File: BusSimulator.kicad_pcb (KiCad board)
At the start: 2 copper layers, 15 parts, among them U1 MPM3620, U2 MPM3620

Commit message: Finished 3v3 and 5V
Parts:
- moved R6 101.2 mm to (114.3, 123.9), turned to 270 degrees
- moved R5 97.3 mm to (114.3, 120.7), turned to 270 degrees
- moved R7 86.7 mm to (117.6, 116.1), turned to 270 degrees
- moved R8 79.0 mm to (114.8, 116.7), turned to 180 degrees
- moved C4 58.7 mm to (126.2, 120.9), turned to 270 degrees
- moved C3 54.3 mm to (122.3, 115.2), turned to 180 degrees
- moved U2 53.3 mm to (118.2, 121.8), turned to 0 degrees
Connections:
- C3 pad 1: Earth -> GNDREF
- C4 pad 1: Earth -> GNDREF
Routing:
- net (no net): track 9.47 -> 37.8 mm, vias 6 -> 2
- net GNDREF: track 13.5 -> 39.7 mm
- net Net-(C1-Pad2): track 8.35 -> 30.4 mm
- net GNDA: track 13.9 -> 29.0 mm
- net +3V3: track 0.00 -> 10.7 mm, vias 0 -> 4
- net Net-(C3-Pad2): track 0.00 -> 8.35 mm
- net Net-(R5-Pad2): track 0.00 -> 4.66 mm
- net Net-(R8-Pad1): track 0.00 -> 3.17 mm
- net Net-(R7-Pad2): track 0.00 -> 2.36 mm
- net +5V: track 25.3 -> 26.9 mm, vias 3 -> 4
- added copper zone on B.Cu, net +3V3
- added copper zone on F.Cu, net +3V3
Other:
- board text added: "Vin"

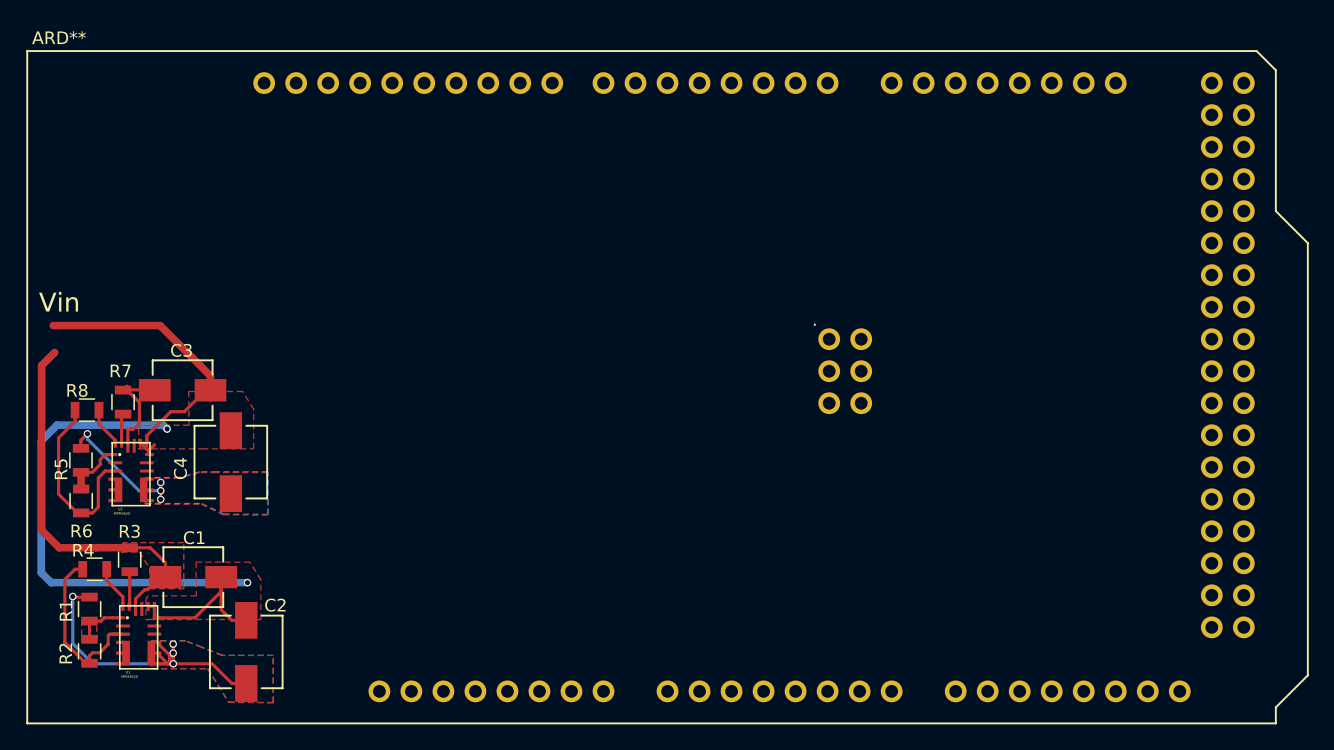
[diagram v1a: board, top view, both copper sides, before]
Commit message: added dc connector and outline pcb
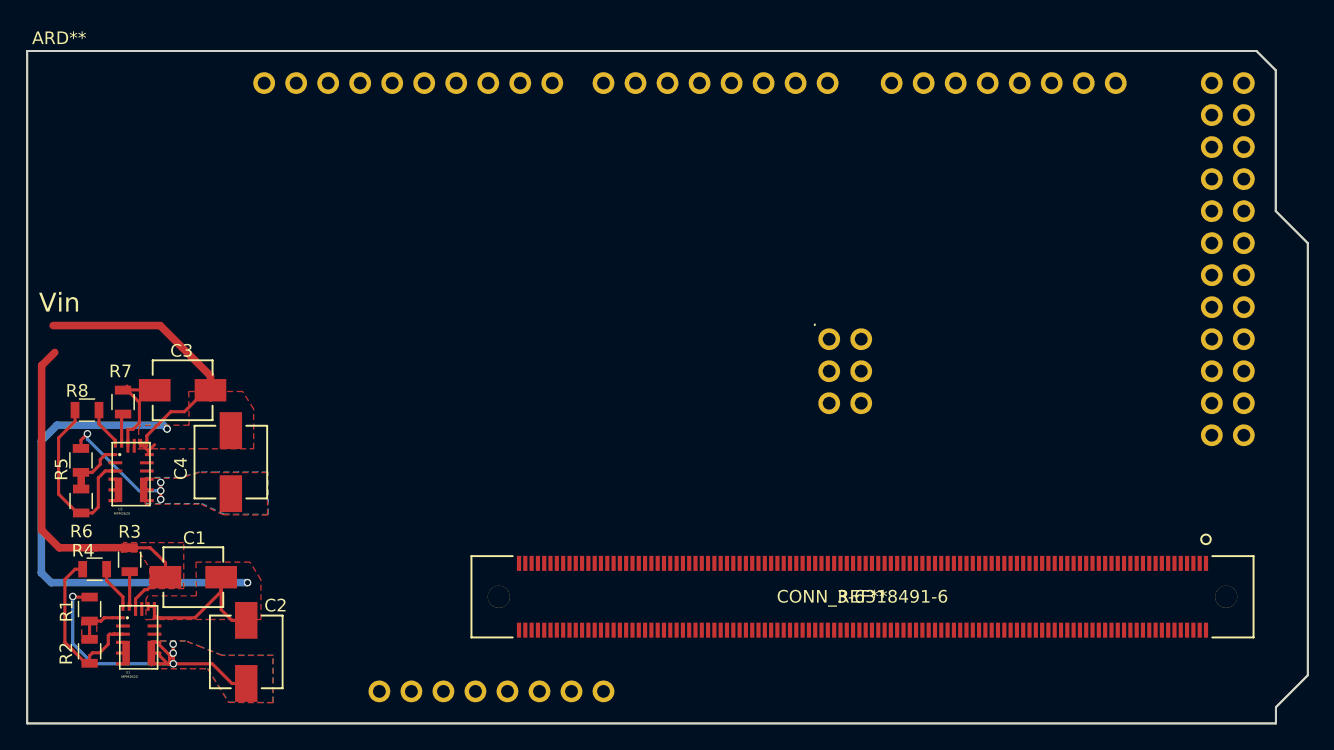
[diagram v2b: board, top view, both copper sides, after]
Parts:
- added REF**: CONN_3-6318491-6, BusSimulator:ComExpressMini10, F.Cu at (211.0, 134.2)
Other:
- board outline added: 101.6 x 53.3 mm

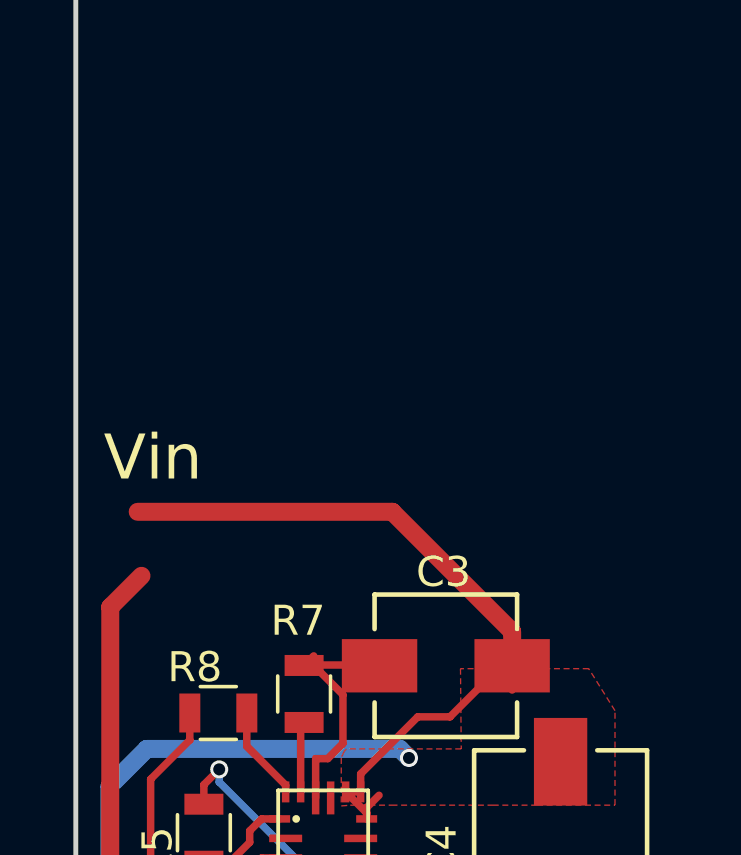
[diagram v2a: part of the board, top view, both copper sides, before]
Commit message: dc jack
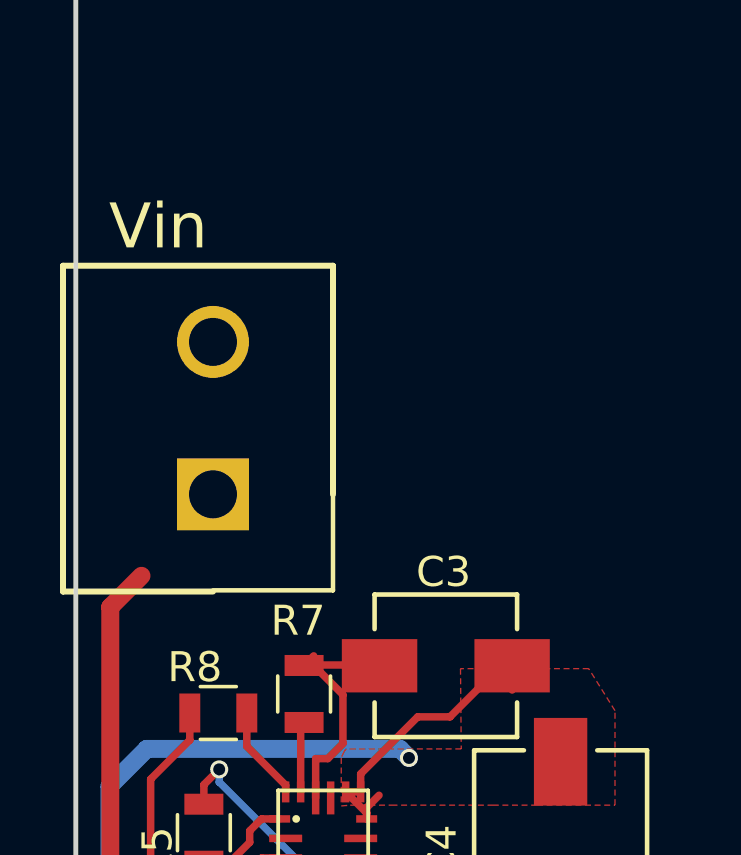
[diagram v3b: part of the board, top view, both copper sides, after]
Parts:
- added J1: , BusSimulator:OSTTA024163, F.Cu at (114.6, 109.5)
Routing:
- net GNDREF: track 39.7 -> 24.4 mm
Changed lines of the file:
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@@
     (thickness 1.6)
     (drawings 10)
-    (tracks 144)
+    (tracks 141)
     (zones 0)
-    (modules 16)
+    (modules 17)
     (nets 23)
   )
@@
     (mod_text_size 1 1)
     (mod_text_width 0.15)
-    (pad_size 1.524 1.524)
-    (pad_drill 0.762)
+    (pad_size 2.4 2.4)
+    (pad_drill 1.6)
     (pad_to_mask_clearance 0.2)
     (aux_axis_origin 0 0)
@@
     (pad 222 thru_hole circle (at 5.871598 2.65 180) (size 1.7526 1.7526) (drill 1.7526) (layers *.Cu F.SilkS))
   )
+  (module BusSimulator:OSTTA024163 (layer F.Cu)
+    (at 114.575 109.45 90)
+    (descr OSTTA024163)
+    (tags Connector)
+    (fp_text reference J1 (at 2.55 -0.15 360) (layer F.SilkS) hide
+      (effects (font (size 1.27 1.27) (thickness 0.254)))
+    )
+    (fp_text value "" (at 0 0 90) (layer F.SilkS) hide
+      (effects (font (size 1.27 1.27) (thickness 0.254)))
+    )
+    (fp_line (start -3.2 0) (end -3.2 4) (layer F.SilkS) (width 0.15))
+    (fp_line (start -3.2 4) (end 1 4) (layer F.SilkS) (width 0.15))
+    (fp_line (start -3.49 4.25) (end -3.49 -5.25) (layer Dwgs.User) (width 0.05))
+    (fp_line (start -3.49 -5.25) (end 7.87 -5.25) (layer Dwgs.User) (width 0.05))
+    (fp_line (start 7.87 -5.25) (end 7.87 4.25) (layer Dwgs.User) (width 0.05))
+    (fp_line (start 7.87 4.25) (end -3.49 4.25) (layer Dwgs.User) (width 0.05))
+    (fp_line (start -3.24 4) (end -3.24 -5) (layer Dwgs.User) (width 0.1))
+    (fp_line (start -3.24 -5) (end 7.62 -5) (layer Dwgs.User) (width 0.1))
+    (fp_line (start 7.62 -5) (end 7.62 4) (layer Dwgs.User) (width 0.1))
+    (fp_line (start 7.62 4) (end -3.24 4) (layer Dwgs.User) (width 0.1))
+    (fp_line (start 0 4) (end 7.62 4) (layer F.SilkS) (width 0.2))
+    (fp_line (start 7.62 4) (end 7.62 -5) (layer F.SilkS) (width 0.2))
+    (fp_line (start 7.62 -5) (end -3.24 -5) (layer F.SilkS) (width 0.2))
+    (fp_line (start -3.24 -5) (end -3.24 0) (layer F.SilkS) (width 0.2))
+    (pad 1 thru_hole rect (at 0 0 180) (size 2.4 2.4) (drill 1.6) (layers *.Cu *.Mask F.SilkS))
+    (pad 2 thru_hole circle (at 5.08 0 180) (size 2.4 2.4) (drill 1.6) (layers *.Cu *.Mask F.SilkS))
+  )
   (gr_line (start 110 141.6) (end 110 88.25) (layer Edge.Cuts) (width 0.15))
   (gr_line (start 209.075 141.6) (end 110 141.6) (layer Edge.Cuts) (width 0.15))
@@
   (gr_line (start 207.525 88.25) (end 209.05 89.775) (layer Edge.Cuts) (width 0.15))
   (gr_line (start 110 88.25) (end 207.525 88.25) (layer Edge.Cuts) (width 0.15))
-  (gr_text "Vin \n" (at 112.5728 108.2294) (layer F.SilkS)
+  (gr_text "Vin \n" (at 112.75 100.525 360) (layer F.SilkS)
     (effects (font (size 1.5 1.5) (thickness 0.3)))
   )
@@
   (segment (start 116.996948 119.144698) (end 115.701948 117.849698) (width 0.25) (layer F.Cu) (net 11))
   (segment (start 115.701948 117.849698) (end 115.701948 116.739698) (width 0.25) (layer F.Cu) (net 11))
-  (segment (start 120.55305 110.0328) (end 112.0648 110.0328) (width 0.6) (layer F.Cu) (net 17))
-  (segment (start 124.546148 115.164898) (end 124.546148 114.025898) (width 0.6) (layer F.Cu) (net 17))
-  (segment (start 124.546148 114.025898) (end 120.55305 110.0328) (width 0.6) (layer F.Cu) (net 17))
   (segment (start 119.696948 119.894698) (end 119.696948 120.269698) (width 0.25) (layer F.Cu) (net 17))
   (segment (start 119.696948 119.894698) (end 120.110046 119.4816) (width 0.25) (layer F.Cu) (net 17))

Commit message: POWER SUPPLY STUFF
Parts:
- J1: value (none) -> CONN_3-6318491-6
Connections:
- C1 pad 2: Net-(C1-Pad2) -> +12V
- C3 pad 2: Net-(C3-Pad2) -> +12V
- J1 pad 1: (no net) -> +12V
- J1 pad 2: (no net) -> GNDREF
- R3 pad 1: Net-(C1-Pad2) -> +12V
- R7 pad 1: Net-(C3-Pad2) -> +12V
- U1 pad 16: Net-(C1-Pad2) -> +12V
- U2 pad 16: Net-(C3-Pad2) -> +12V
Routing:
- net +12V: track 0.00 -> 52.2 mm
- net GNDREF: track 24.4 -> 58.9 mm
- net Net-(C1-Pad2): track 30.4 -> 0.00 mm
- net (no net): track 37.8 -> 53.7 mm, vias 2 -> 4
- net Net-(C3-Pad2): track 8.35 -> 0.00 mm
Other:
- net class Default: trace_width 0.25 -> 0.6

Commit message: CONNECTOR MAPPED
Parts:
- renumbered REF** to J1, J1 to J2
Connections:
- J1 pad 1: (no net) -> GND
- J1 pad 10: (no net) -> GBE0_MDI1+
- J1 pad 100: (no net) -> GND
- J1 pad 101: (no net) -> Net-(J1-Pad101)
- J1 pad 102: (no net) -> Net-(J1-Pad102)
- J1 pad 103: (no net) -> LIDn
- J1 pad 104: (no net) -> VCC_12V
- J1 pad 105: (no net) -> VCC_12V
- J1 pad 106: (no net) -> VCC_12V
- J1 pad 107: (no net) -> VCC_12V
- J1 pad 108: (no net) -> VCC_12V
- J1 pad 109: (no net) -> VCC_12V
- J1 pad 11: (no net) -> GND
- J1 pad 110: (no net) -> GND
- J1 pad 111: (no net) -> GND
- J1 pad 112: (no net) -> GBE0_ACTn
- J1 pad 113: (no net) -> Net-(J1-Pad113)
- J1 pad 114: (no net) -> Net-(J1-Pad114)
- J1 pad 115: (no net) -> Net-(J1-Pad115)
- J1 pad 116: (no net) -> Net-(J1-Pad116)
- J1 pad 117: (no net) -> Net-(J1-Pad117)
- J1 pad 118: (no net) -> Net-(J1-Pad118)
- J1 pad 119: (no net) -> Net-(J1-Pad119)
- J1 pad 12: (no net) -> GBE0_MDI0-
- J1 pad 120: (no net) -> Net-(J1-Pad120)
- J1 pad 121: (no net) -> GND
- J1 pad 122: (no net) -> PWRBTNn
- J1 pad 123: (no net) -> Net-(J1-Pad123)
- J1 pad 124: (no net) -> Net-(J1-Pad124)
- J1 pad 125: (no net) -> Net-(J1-Pad125)
- J1 pad 126: (no net) -> Net-(J1-Pad126)
- J1 pad 127: (no net) -> Net-(J1-Pad127)
- J1 pad 128: (no net) -> Net-(J1-Pad128)
- J1 pad 129: (no net) -> Net-(J1-Pad129)
- J1 pad 13: (no net) -> GBE0_MDI0+
- J1 pad 130: (no net) -> Net-(J1-Pad130)
- J1 pad 131: (no net) -> GND
- J1 pad 132: (no net) -> USB_SSTX0-
- J1 pad 133: (no net) -> USB_SSTX0+
- J1 pad 134: (no net) -> PWR_OK
- J1 pad 135: (no net) -> Net-(J1-Pad135)
- J1 pad 136: (no net) -> Net-(J1-Pad136)
- J1 pad 137: (no net) -> Net-(J1-Pad137)
- J1 pad 138: (no net) -> Net-(J1-Pad138)
- J1 pad 139: (no net) -> Net-(J1-Pad139)
- J1 pad 14: (no net) -> GBE0_CTREF(GND)
- J1 pad 140: (no net) -> AC/HDA_SDIN0
- J1 pad 141: (no net) -> GND
- J1 pad 142: (no net) -> Net-(J1-Pad142)
- J1 pad 143: (no net) -> I2C_CK
- J1 pad 144: (no net) -> I2C_DAT
- J1 pad 145: (no net) -> THRMn
- J1 pad 146: (no net) -> Net-(J1-Pad146)
- J1 pad 147: (no net) -> Net-(J1-Pad147)
- J1 pad 148: (no net) -> USB_4_5_OCn
- J1 pad 149: (no net) -> USB5-
- J1 pad 15: (no net) -> Net-(J1-Pad15)
- J1 pad 150: (no net) -> USB5+
- J1 pad 151: (no net) -> GND
- J1 pad 152: (no net) -> USB3-
- J1 pad 153: (no net) -> USB3+
- J1 pad 154: (no net) -> USB_0_1_OCn
- J1 pad 155: (no net) -> USB1-
- J1 pad 156: (no net) -> USB1+
- J1 pad 157: (no net) -> Net-(J1-Pad157)
- J1 pad 158: (no net) -> EXCD1_CPPEn
- J1 pad 159: (no net) -> SYS_RESETn
- J1 pad 16: (no net) -> SATA0_TX+
- J1 pad 160: (no net) -> CB_RESETn
- J1 pad 161: (no net) -> GND
- J1 pad 162: (no net) -> Net-(J1-Pad162)
- J1 pad 163: (no net) -> Net-(J1-Pad163)
- J1 pad 164: (no net) -> GPO1
- J1 pad 165: (no net) -> Net-(J1-Pad165)
- J1 pad 166: (no net) -> Net-(J1-Pad166)
- J1 pad 167: (no net) -> GPO2
- J1 pad 168: (no net) -> Net-(J1-Pad168)
- J1 pad 169: (no net) -> Net-(J1-Pad169)
- J1 pad 17: (no net) -> SATA0_TX-
- J1 pad 170: (no net) -> GND
- J1 pad 171: (no net) -> Net-(J1-Pad171)
- J1 pad 172: (no net) -> Net-(J1-Pad172)
- J1 pad 173: (no net) -> GPO3
- J1 pad 174: (no net) -> PCIE_RX1+
- J1 pad 175: (no net) -> PCIE_RX1-
- J1 pad 176: (no net) -> WAKE0n
- J1 pad 177: (no net) -> WAKE1n
- J1 pad 178: (no net) -> PCIE_RX0+
- J1 pad 179: (no net) -> PCIE_RX0-
- J1 pad 18: (no net) -> Net-(J1-Pad18)
- J1 pad 180: (no net) -> GND
- J1 pad 181: (no net) -> DDIO_PAIR0+
- J1 pad 182: (no net) -> DDIO_PAIR0-
- J1 pad 183: (no net) -> DDIO_PAIR1+
- J1 pad 184: (no net) -> DDIO_PAIR1-
- J1 pad 185: (no net) -> DDIO_PAIR2+
- J1 pad 186: (no net) -> DDIO_PAIR2-
- J1 pad 187: (no net) -> Net-(J1-Pad187)
- J1 pad 188: (no net) -> Net-(J1-Pad188)
- J1 pad 189: (no net) -> LVDS_BKLT_EN
- J1 pad 19: (no net) -> SATA0_RX+
- J1 pad 190: (no net) -> GND
- J1 pad 191: (no net) -> DDIO_PAIR3+
- J1 pad 192: (no net) -> DDIO_PAIR3-
- J1 pad 193: (no net) -> LVDS_BKLT_CTRL
- J1 pad 194: (no net) -> VCC_5V_SBY
- J1 pad 195: (no net) -> VCC_5V_SBY
- J1 pad 196: (no net) -> VCC_5V_SBY
- J1 pad 197: (no net) -> VCC_5V_SBY
- J1 pad 198: (no net) -> Net-(J1-Pad198)
- J1 pad 199: (no net) -> DDIO_HPD
- J1 pad 2: (no net) -> GBE0_MDI3-
- J1 pad 20: (no net) -> SATA0_RX-
- J1 pad 200: (no net) -> GND
- J1 pad 201: (no net) -> Net-(J1-Pad201)
- J1 pad 202: (no net) -> Net-(J1-Pad202)
- J1 pad 203: (no net) -> Net-(J1-Pad203)
- J1 pad 204: (no net) -> Net-(J1-Pad204)
- J1 pad 205: (no net) -> DDIO_DDC_AUX_SEL
- J1 pad 206: (no net) -> Net-(J1-Pad206)
- J1 pad 207: (no net) -> SPI_CSn
- J1 pad 208: (no net) -> DDIO_CTRLCLK_AUX+
- J1 pad 209: (no net) -> DDIO_CTRLDATA_AUX-
- J1 pad 21: (no net) -> GND
- J1 pad 210: (no net) -> GND
- J1 pad 211: (no net) -> FAN_PWMOUTn
- J1 pad 212: (no net) -> FAN_TACHINn
- J1 pad 213: (no net) -> SLEEPn
- J1 pad 214: (no net) -> VCC_12V
- J1 pad 215: (no net) -> VCC_12V
- J1 pad 216: (no net) -> VCC_12V
- J1 pad 217: (no net) -> VCC_12V
- J1 pad 218: (no net) -> VCC_12V
- J1 pad 219: (no net) -> VCC_12V
- J1 pad 22: (no net) -> USB_SSRX0-
- J1 pad 220: (no net) -> GND
- J1 pad 23: (no net) -> USB_SSRX0+
- J1 pad 24: (no net) -> Net-(J1-Pad24)
- J1 pad 25: (no net) -> Net-(J1-Pad25)
- J1 pad 26: (no net) -> Net-(J1-Pad26)
- J1 pad 27: (no net) -> BATLOWn
- J1 pad 28: (no net) -> SATA_ACTn
- J1 pad 29: (no net) -> AC/HDA_SYNC
- J1 pad 3: (no net) -> GBE0_MDI3+
- J1 pad 30: (no net) -> Net-(J1-Pad30)
- J1 pad 31: (no net) -> GND
- J1 pad 32: (no net) -> AC/HDA_BITCLK
- J1 pad 33: (no net) -> AC/HDA_SDOUT
- J1 pad 34: (no net) -> Net-(J1-Pad34)
- J1 pad 35: (no net) -> Net-(J1-Pad35)
- J1 pad 36: (no net) -> Net-(J1-Pad36)
- J1 pad 37: (no net) -> Net-(J1-Pad37)
- J1 pad 38: (no net) -> Net-(J1-Pad38)
- J1 pad 39: (no net) -> USB4-
- J1 pad 4: (no net) -> GBE0_LINK100n
- J1 pad 40: (no net) -> USB4+
- J1 pad 41: (no net) -> GND
- J1 pad 42: (no net) -> USB2-
- J1 pad 43: (no net) -> USB2+
- J1 pad 44: (no net) -> USB_2_3_OCn
- J1 pad 45: (no net) -> USB0-
- J1 pad 46: (no net) -> USB0+
- J1 pad 47: (no net) -> VCC_RTC
- J1 pad 48: (no net) -> Net-(J1-Pad48)
- J1 pad 49: (no net) -> EXCD0_CPPEn
- J1 pad 5: (no net) -> GBE0_LINK1000n
- J1 pad 50: (no net) -> Net-(J1-Pad50)
- J1 pad 51: (no net) -> GND
- J1 pad 52: (no net) -> Net-(J1-Pad52)
- J1 pad 53: (no net) -> Net-(J1-Pad53)
- J1 pad 54: (no net) -> GPI0
- J1 pad 55: (no net) -> Net-(J1-Pad55)
- J1 pad 56: (no net) -> Net-(J1-Pad56)
- J1 pad 57: (no net) -> GND
- J1 pad 58: (no net) -> Net-(J1-Pad58)
- J1 pad 59: (no net) -> Net-(J1-Pad59)
- J1 pad 6: (no net) -> GBE0_MDI2-
- J1 pad 60: (no net) -> GND
- J1 pad 61: (no net) -> Net-(J1-Pad61)
- J1 pad 62: (no net) -> Net-(J1-Pad62)
- J1 pad 63: (no net) -> GPI1
- J1 pad 64: (no net) -> PCIE_TX1+
- J1 pad 65: (no net) -> PCIE_TX1-
- J1 pad 66: (no net) -> GND
- J1 pad 67: (no net) -> GPI2
- J1 pad 68: (no net) -> PCIE_TX0+
- J1 pad 69: (no net) -> PCIE_TX0-
- J1 pad 7: (no net) -> GBE0_MDI2+
- J1 pad 70: (no net) -> GND
- J1 pad 71: (no net) -> LVDS_A0+
- J1 pad 72: (no net) -> LVDS_A0-
- J1 pad 73: (no net) -> LVDS_A1+
- J1 pad 74: (no net) -> LVDS_A1-
- J1 pad 75: (no net) -> LVDS_A2+
- J1 pad 76: (no net) -> LVDS_A2-
- J1 pad 77: (no net) -> LVD_VDD_EN
- J1 pad 78: (no net) -> LVDS_A3+
- J1 pad 79: (no net) -> LVDS_A3-
- J1 pad 8: (no net) -> Net-(J1-Pad8)
- J1 pad 80: (no net) -> GND
- J1 pad 81: (no net) -> LVDS_A_CK+
- J1 pad 82: (no net) -> LVDS_A_CK-
- J1 pad 83: (no net) -> LVDS_I2C_CK
- J1 pad 84: (no net) -> LDVS_I2C_DAT
- J1 pad 85: (no net) -> GPI3
- J1 pad 86: (no net) -> Net-(J1-Pad86)
- J1 pad 87: (no net) -> eDP_HPD
- J1 pad 88: (no net) -> PCIE_CLK_REF+
- J1 pad 89: (no net) -> PCIE_CLK_REF-
- J1 pad 9: (no net) -> GBE0_MDI1-
- J1 pad 90: (no net) -> GND
- J1 pad 91: (no net) -> SPI_POWER
- J1 pad 92: (no net) -> SPI_MISO
- J1 pad 93: (no net) -> GPO0
- J1 pad 94: (no net) -> SPI_CLK
- J1 pad 95: (no net) -> SPI_MOSI
- J1 pad 96: (no net) -> Net-(J1-Pad96)
- J1 pad 97: (no net) -> TYPE10n(GND)
- J1 pad 98: (no net) -> SER0_TX
- J1 pad 99: (no net) -> SER0_RX

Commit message: schematic build voltage sense
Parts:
- moved J1 87.0 mm to (133.8, 94.2), turned to 0 degrees
